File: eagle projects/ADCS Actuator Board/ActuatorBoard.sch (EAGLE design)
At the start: 155 parts, among them J19 TE_1-84953-1, J20 TE_1-84953-1, J21 TE_1-84953-1, J7 CNC_3221-10-0300-00, J8 CNC_3221-14-0300-00, U1 TVS991, U10 DRV10970_MOTOR_DRIVERDRV10970, U12 DRV10970_MOTOR_DRIVERDRV10970, U2 ADS7841E_2K5, U3 ADS7841E_2K5, U35 BD6210F-E2, U39 BD6210F-E2, U5 TVS991, U7 DRV10970_MOTOR_DRIVERDRV10970, U8 TVS991, U9 BD6210F-E2

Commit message: Staring REV B Act board
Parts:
- removed C119, C121, C122, C126, C129, C130, C139, C142, C25, C26: 0.1u, rcl:C-EUC0603
- removed C120, C140: 1u, rcl:C-EUC0603
- removed C123, C131: 0.1u, rcl:C-EUC0402
- removed C125, C141: 0.33u, rcl:C-EUC0603
- removed C127, C143: 2.2u, rcl:C-EUC0603
- removed C128, C144: 10u, rcl:C-EUC0603
- removed J19, J20, J21: TE_1-84953-1, my_library:TE_1-84953-1
- removed J5: (no value), my_library:PINHD-1X3
- removed JP7, JP9: (no value), my_library:JP1Q_
- removed JX, JY, JZ: (no value), my_library:TRM_BLK_1X2
- removed R23: 100R, rcl:R-US_M0805
- removed R28, R29, R37, R38, R5: 1.8k, rcl:R-US_R0402
- removed R3, R4, R76: 5.1k, rcl:R-US_R0402
- removed R73, R74: 3.3k, rcl:R-US_R0603
- removed TP35, TP36, TP43, TP44, TP46, TP54, TP7: TESTPOINT, my_library:TESTPOINT
- removed U1: TVS991, my_library:TVS991
- removed U35, U39, U9: BD6210F-E2, my_library:BD6210F-E2
- added C1, C11, C2, C20, C34, C45, C50, C51, C54, C58, C63: 0.1u, rcl:C-EUC0603
- added C10, C3, C4, C46, C52, C6, C8: 0.1u, rcl:C-EUC0402
- added C12, C32, C55, C62: 1u, rcl:C-EUC0603
- added C19, C57: 0.33u, rcl:C-EUC0603
- added C28, C35, C59: 2.2u, rcl:C-EUC0603
- added C30, C36, C60: 10u, rcl:C-EUC0603
- added C31, C38, C61: 0.01u, rcl:C-EUC0603
- added C5, C7, C9: 1u, rcl:C-EUC0402
- added J11, J2: TE_1-84953-1, my_library:TE_1-84953-1
- added J12, J3: (no value), my_library:PINHD-1X3
- added JP2, JP3: (no value), pinhead:PINHD-1X2
- added R102, R103, R59, R60: 10K, rcl:R-US_R0603
- added R104, R61: 75K, rcl:R-US_R0603
- added R105, R106, R62, R63: 3.3k, rcl:R-US_R0603
- added R107, R108, R109, R64, R65, R66: 4.7k, rcl:R-US_R0402
- added R110, R111, R112, R113, R114, R115, R58, R67, R68, R69, R70, R71, R75: 5.1M, rcl:R-US_R0402
- added R116, R77: 10k, rcl:R-US_R0603
- added R117, R78: 2k, rcl:R-US_R0603
- added R118, R79: 1k, rcl:R-US_R0603
- added R119, R80: 100k, rcl:R-US_R0603
- added R47, R89: 0R, rcl:R-US_M0805
- added R57: 10K, rcl:R-US_R0402
- added R81: 5.1k, rcl:R-US_R0402
- added R82: 100R, rcl:R-US_M0805
- added R88: DNP, rcl:R-US_M0805
- added TP1, TP10, TP11, TP12, TP13, TP14, TP15, TP16, TP17, TP18, TP19, TP20, TP26, TP27, TP28, TP29, TP33, TP37, TP38, TP39, TP47, TP48, TP49, TP50, TP53, TP55, TP56, TP57, TP58, TP59, TP60, TP61, TP62, TP63, TP8, TP9: TESTPOINT, my_library:TESTPOINT
- added U11, U18: BD6210F-E2, my_library:BD6210F-E2
- added U13, U17: LM2917MX/NOPB, my_library:LM2917MX/NOPB
- added U16, U6: DRV10970_MOTOR_DRIVERDRV10970, my_library:DRV10970_MOTOR_DRIVERDRV10970
- added U19: TSV991AILT, my_library:TSV991AILT
- added U4: ADS7841E_2K5, my_library:ADS7841E_2K5
- C27: device rcl:C-EUC0402 -> rcl:C-EUC0603
- C41: value 2.2u -> 1u
- C42: value 10u -> 0.1u
- J4: value (none) -> TE_1-84953-1; device my_library:PINHD-1X3 -> my_library:TE_1-84953-1
- JP5: device my_library:JP1Q_ -> pinhead:PINHD-1X2
- R1, R2: value 4.7k -> 10K; device rcl:R-US_R0402 -> rcl:R-US_R0603
- R11: value 4.7k -> 100R; device rcl:R-US_R0402 -> rcl:R-US_M0805
- R12: value 4.7k -> 5.1k
- R15: value 4.7k -> 1.8k
- R16: value 100R -> 1.8k; device rcl:R-US_M0805 -> rcl:R-US_R0402
- R17: value 5.1k -> 1.8k
- R19, R20: value 10K -> 4.7k; device rcl:R-US_R0603 -> rcl:R-US_R0402
- R21: value 75K -> 5.1M; device rcl:R-US_R0603 -> rcl:R-US_R0402
- R22: value 100R -> DNP
- R24: value 1.8k -> 0R; device rcl:R-US_R0402 -> rcl:R-US_M0805
- R25, R31: value 1.8k -> 5.1k
- R30: value 5.1k -> 100R; device rcl:R-US_R0402 -> rcl:R-US_M0805
- R35, R36: value 3.3k -> 5.1M; device rcl:R-US_R0603 -> rcl:R-US_R0402
- R41: value 5.1M -> 1.8k
- R42: value 5.1M -> DNP; device rcl:R-US_R0402 -> rcl:R-US_M0805
- R44: value 5.1M -> 10k; device rcl:R-US_R0402 -> rcl:R-US_R0603
- R48: value 10K -> 2k
- R49: value 10K -> 1k
- R7: value 4.7k -> 75K; device rcl:R-US_R0402 -> rcl:R-US_R0603
- R72: value 75K -> 100k
- R8, R9: value 4.7k -> 3.3k; device rcl:R-US_R0402 -> rcl:R-US_R0603
- R83: value 10K -> 5.1k; device rcl:R-US_R0603 -> rcl:R-US_R0402
- R84: value 10K -> 1.8k; device rcl:R-US_R0603 -> rcl:R-US_R0402
- R85: value 75K -> 1.8k; device rcl:R-US_R0603 -> rcl:R-US_R0402
- R86, R87: value 3.3k -> 1.8k; device rcl:R-US_R0603 -> rcl:R-US_R0402
- U10: value DRV10970_MOTOR_DRIVERDRV10970 -> LM2917MX/NOPB; device my_library:DRV10970_MOTOR_DRIVERDRV10970 -> my_library:LM2917MX/NOPB
- U12: value DRV10970_MOTOR_DRIVERDRV10970 -> TSV991AILT; device my_library:DRV10970_MOTOR_DRIVERDRV10970 -> my_library:TSV991AILT
- U5: value TVS991 -> BD6210F-E2; device my_library:TVS991 -> my_library:BD6210F-E2
- U8: value TVS991 -> TSV991AILT; device my_library:TVS991 -> my_library:TSV991AILT
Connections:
- removed net MAG_CUR_SEN_Y: R22.2, R30.2, U35.OUT1
- removed net MAG_CUR_SEN_Z: R16.2, R17.2, U39.OUT1
- removed net MAG_Y_FIN: TP43.TP, U35.FIN
- removed net N$10: R28.2, R76.1, U1.IN+
- removed net N$105: C139.1, U12.CPP
- removed net N$106: C140.2, U12.VCP
- removed net N$107: C139.2, U12.CPN
- removed net N$108: C143.1, U12.VINT
- removed net N$109: C141.1, U12.RETRY
- removed net N$18: R28.1, R37.1, R38.2
- removed net N$19 (its old number): R40.2, U10.DAA
- removed net N$23 (its old number): R43.1, U10.CMTMOD
- removed net N$3 (its old number): R39.2, U7.DAA
- removed net N$33: JP7.2, U35.OUT2
- removed net N$4: R5.1, R6.1, U8.IN-
- removed net N$67: JP9.2, U39.OUT2
- removed net N$7: R29.1, R4.1, U1.IN-
- removed net N$87: C119.1, U10.CPP
- removed net N$88: C120.2, U10.VCP
- removed net N$89: C119.2, U10.CPN
- removed net N$90: C127.1, U10.VINT
- removed net N$91: C125.1, U10.RETRY
- removed net OUT1_Y: JY.1, R22.1, R3.2
- removed net OUT1_Z: JZ.1, R16.1, R23.1, R4.2, R6.2
- removed net OUT2_Y: JP7.1, JY.2
- removed net OUT2_Z: JP9.1, JZ.2
- new net !CS!_SPD_SENSE_RW: J7.1, U4.!CS
- new net N$28: R21.2, U7.DAA
- new net N$29: R35.1, U7.CMTMOD
- new net N$30: C41.2, R72.2, TP13.TP, U10.CP2, U10.IN+
- new net N$31: R48.1, R49.2, U10.TACH-
- new net N$32: C8.1, R57.1, U4.!SHDN
- new net N$34: TP1.TP, U4.CH3
- new net N$35: R58.2, U4.BUSY
- new net N$36: C11.1, U6.CPP
- new net N$38: C12.2, U6.VCP
- new net N$39: C11.2, U6.CPN
- new net N$40: C28.1, U6.VINT
- new net N$41: C19.1, U6.RETRY
- new net N$43: R67.2, U6.DAA
- new net N$44: R68.1, U6.CMTMOD
- new net N$49: C32.2, R80.2, TP28.TP, U13.CP2, U13.IN+
- new net N$50: R78.1, R79.2, U13.TACH-
- new net N$51: C31.2, U13.CP1
- new net N$52: C38.2, U10.CP1
- new net N$53: R81.1, R84.2, U19.IN+
- new net N$54: R84.1, R86.1, R87.2
- new net N$55: R82.2, R88.2, R89.1
- new net N$63: C54.1, U16.CPP
- new net N$64: C55.2, U16.VCP
- new net N$65: C54.2, U16.CPN
- new net N$66: C59.1, U16.VINT
- new net N$68: C57.1, U16.RETRY
- new net N$69: R110.2, U16.DAA
- new net N$70: R111.1, U16.CMTMOD
- new net N$72: R117.1, R118.2, U17.TACH-
- new net N$73: C61.2, U17.CP1
- new net RW_X_SPD: R44.2, TP12.TP, U10.EMIT, U10.IN-, U4.CH1
- new net RW_Y_SPD: R116.2, TP56.TP, U17.EMIT, U17.IN-, U4.CH0
- new net RW_Z_SPD: R77.2, TP27.TP, U13.EMIT, U13.IN-, U4.CH2
- new net X_DNC_1: R36.1, U10.DNC_1
- new net X_DNC_2: R39.1, U10.DNC_2
- new net X_DNC_3: R43.1, U10.DNC_3
- new net X_DNC_4: R40.1, U10.DNC_4
- new net Y_DNC_1: R112.1, U17.DNC_1
- new net Y_DNC_2: R113.1, U17.DNC_2
- new net Y_DNC_3: R115.1, U17.DNC_3
- new net Y_DNC_4: R114.1, U17.DNC_4
- new net Z_DNC_1: R69.1, U13.DNC_1
- new net Z_DNC_2: R70.1, U13.DNC_2
- new net Z_DNC_3: R75.1, U13.DNC_3
- new net Z_DNC_4: R71.1, U13.DNC_4
- net +3V3: now also C10.1, C34.2, C4.1, C42.2, C5.1, C6.1, C63.2, C7.1, C9.1, R105.1, R106.1, R118.1, R17.2, R34.2, R49.1, R57.2, R62.1, R63.1, R79.1, R8.1, R86.2, R9.1, U10.COL, U10.V+, U13.COL, U13.V+, U17.COL, U17.V+, U4.VCC+, U4.VCC+_2, U4.VREF; no longer R31.2, R33.2, R35.1, R36.1, R37.2, R73.1, R74.1, R86.1, R87.1
- net +5V: now also C1.1, C12.1, C2.2, C3.1, C30.1, C36.1, C45.2, C46.1, C50.1, C51.2, C52.1, C55.1, C60.1, J11.1, J12.3, J2.1, J3.3, J4.1, R102.2, R107.2, R108.2, R109.2, R20.2, R59.2, R64.2, R65.2, R66.2, U11.VCC_1, U11.VCC_2, U11.VREF, U12.VCC, U16.VM, U18.VCC_1, U18.VCC_2, U18.VREF, U19.VCC, U5.VCC_1, U5.VCC_2, U5.VREF, U6.VM; no longer C120.1, C121.1, C122.2, C123.1, C128.1, C129.1, C130.2, C131.1, C140.1, C144.1, C25.1, C26.2, C42.1, J19.1, J20.1, J21.1, J4.3, J5.3, R11.2, R12.2, R15.2, R2.2, R48.2, R7.2, R8.2, R83.2, R9.2, U1.VCC, U10.VM, U12.VM, U35.VCC_1, U35.VCC_2, U35.VREF, U39.VCC_1, U39.VCC_2, U39.VREF, U5.VCC, U9.VCC_1, U9.VCC_2, U9.VREF
- net BRKMOD_X: now also J6.2, U7.BRKMOD; no longer J4.2, U10.BRKMOD
- net BRKMOD_Y: now also J12.2, U16.BRKMOD; no longer J6.2, U7.BRKMOD
- net BRKMOD_Z: now also J3.2, U6.BRKMOD; no longer J5.2, U12.BRKMOD
- net CUR_OUT1: no longer R5.2, U8.OUT
- net CUR_OUT2: no longer R24.2, TP46.TP, U5.OUT
- net CUR_OUT3: now also R16.2, R33.2, R85.2, TP10.TP, TP30.TP, TP51.TP, U12.OUT, U19.OUT, U8.OUT; no longer R29.2, TP54.TP, U1.OUT
- net GND: now also C1.2, C10.2, C19.2, C2.1, C20.2, C28.2, C3.2, C30.2, C31.1, C32.1, C34.1, C35.2, C36.2, C38.1, C4.2, C41.1, C42.1, C45.1, C46.2, C5.2, C50.2, C51.1, C52.2, C57.2, C58.2, C59.2, C6.2, C60.2, C61.1, C62.1, C63.1, C7.2, C8.2, C9.2, J11.5, J11.TAB1, J11.TAB2, J12.1, J2.5, J2.TAB1, J2.TAB2, J3.1, J4.5, J4.TAB1, J4.TAB2, R103.1, R104.1, R110.1, R111.2, R112.2, R113.2, R114.2, R115.2, R116.1, R117.2, R119.1, R18.1, R2.1, R35.2, R36.2, R39.2, R40.2, R44.1, R48.2, R58.1, R60.1, R61.1, R67.1, R68.2, R69.2, R7.1, R70.2, R71.2, R75.2, R77.1, R78.2, R80.1, R87.1, U11.GND, U12.VSS, U13.GND, U16.GND, U16.THERMALPAD, U17.GND, U18.GND, U19.VSS, U4.COM, U4.GND, U4.MODE, U5.GND, U6.GND, U6.THERMALPAD; no longer C121.2, C122.1, C123.2, C125.2, C126.2, C127.2, C128.2, C129.2, C130.1, C131.2, C141.2, C142.2, C143.2, C144.2, C25.2, C26.1, C41.2, C42.2, J19.5, J19.TAB1, J19.TAB2, J20.5, J20.TAB1, J20.TAB2, J21.5, J21.TAB1, J21.TAB2, J4.1, J5.1, R20.1, R32.1, R34.1, R38.1, R39.1, R40.1, R42.2, R44.2, R49.1, R84.1, R85.1, U1.VSS, U10.THERMALPAD, U12.GND, U12.THERMALPAD, U35.GND, U39.GND, U5.VSS, U9.GND
- net MAG_CUR_SEN_X: now also R24.2, R25.2, R47.2, R6.2, R81.2, R89.2, TP17.TP, TP34.TP, TP52.TP, U11.OUT1, U18.OUT1, U5.OUT1; no longer R23.2, R76.2, U9.OUT1
- net MAG_X_FIN: now also TP24.TP, TP47.TP, TP8.TP, U11.FIN, U18.FIN, U5.FIN; no longer TP35.TP, U9.FIN
- net MAG_X_RIN: now also TP25.TP, TP48.TP, TP9.TP, U11.RIN, U18.RIN, U5.RIN; no longer TP36.TP, U9.RIN
- net MAG_Y_RIN: no longer TP44.TP, U35.RIN
- net MAG_Z_FIN: no longer TP51.TP, U39.FIN
- net MAG_Z_RIN: no longer TP52.TP, U39.RIN
- net N$16: now also R11.2, R22.2, R24.1; no longer JP5.2, U9.OUT2
- net N$17: now also R31.1, U12.IN-; no longer R34.2
- net N$20: now also R25.1, R32.2, U12.IN+; no longer R41.2, U12.DAA
- net N$21: now also R32.1, R34.1, R41.2; no longer R18.1, R31.1, R32.2
- net N$22: now also R30.2, R42.2, R47.1; no longer R42.1, U12.CMTMOD
- net N$24: now also C35.1, U7.VINT; no longer R44.1, U7.CMTMOD
- net N$48: now also R83.1, R85.1, U19.IN-; no longer R25.1
- net N$6: now also R12.1, R16.1, U8.IN-; no longer R24.1, R3.1, U5.IN-
- net N$71: now also C62.2, R119.2, TP57.TP, U17.CP2, U17.IN+; no longer C41.1, U7.VINT
- net N$8: now also R15.2, R6.1; no longer R17.1, R18.2
- net N$9: now also R15.1, R17.1, R18.2; no longer R25.2, R30.1, U5.IN+
- net OUT1_X: now also JP2.1, JP3.1, JP5.1, R11.1, R12.2, R22.1, R30.1, R31.2, R42.1, R82.1, R83.2, R88.1, TP21.TP, TP39.TP, TP62.TP; no longer JX.1
- net OUT2_X: now also JP2.2, JP3.2, JP5.2, TP22.TP, TP40.TP, TP63.TP, U11.OUT2, U18.OUT2, U5.OUT2; no longer JP5.1, JX.2
- net RW_X_DIR: now also U7.FR; no longer U10.FR
- net RW_X_I_SENS: now also R7.2, TP11.TP, U7.CS; no longer R72.2, TP34.TP, U10.CS
- net RW_X_LOCK: now also R9.2, U7.RD; no longer R74.2, U10.RD
- net RW_X_OUTFG: now also R8.2, TP23.TP, U10.TACH+, U7.FG; no longer J8.13, R73.2, U10.FG
- net RW_X_SPEED_CTRL: now also U7.PWM; no longer U10.PWM
- net RW_Y_DIR: now also U16.FR; no longer U7.FR
- net RW_Y_I_SENS: now also R104.2, TP55.TP, U16.CS; no longer R21.2, TP30.TP, U7.CS
- net RW_Y_LOCK: now also R106.2, U16.RD; no longer R36.2, U7.RD
- net RW_Y_OUTFG: now also R105.2, TP61.TP, U16.FG, U17.TACH+; no longer J7.1, R35.2, U7.FG
- net RW_Y_SPEED_CTRL: now also U16.PWM; no longer U7.PWM
- net RW_Z_DIR: now also U6.FR; no longer U12.FR
- net RW_Z_I_SENS: now also R61.2, TP26.TP, U6.CS; no longer R85.2, TP40.TP, U12.CS
- net RW_Z_LOCK: now also R63.2, U6.RD; no longer R87.2, U12.RD
- net RW_Z_OUTFG: now also R62.2, TP38.TP, U13.TACH+, U6.FG; no longer J7.2, R86.2, U12.FG
- net RW_Z_SPEED_CTRL: now also U6.PWM; no longer U12.PWM
- net UCB0_SPI_CLK: now also U4.DCLK
- net UCB0_SPI_MISO: now also U4.DOUT
- net UCB0_SPI_MOSI: now also U4.DIN
- net VINT/2_X: now also C16.1, R1.1, R2.2, U7.U_HN, U7.V_HN, U7.W_HN; no longer C126.1, R48.1, R49.2, U10.U_HN, U10.V_HN, U10.W_HN
- net VINT/2_Y: now also C58.1, R102.1, R103.2, U16.U_HN, U16.V_HN, U16.W_HN; no longer C16.1, R19.1, R20.2, U7.U_HN, U7.V_HN, U7.W_HN
- net VINT/2_Z: now also C20.1, R59.1, R60.2, U6.U_HN, U6.V_HN, U6.W_HN; no longer C142.1, R83.1, R84.2, U12.U_HN, U12.V_HN, U12.W_HN
- net X_HALL_A: now also J4.3, R19.1, U7.U_HP; no longer J19.3, R2.1, U10.U_HP
- net X_HALL_B: now also J4.4, R10.1, U7.V_HP; no longer J19.4, R1.1, U10.V_HP
- net X_HALL_C: now also J4.2, R20.1, U7.W_HP; no longer J19.2, R7.1, U10.W_HP
- net X_PHASE_A: now also J4.10, J4.11, TP14.TP, U7.U; no longer J19.10, J19.11, U10.U
- net X_PHASE_B: now also J4.8, J4.9, TP15.TP, U7.V; no longer J19.8, J19.9, U10.V
- net X_PHASE_C: now also U7.W; no longer J19.6, J19.7, U10.W
- net Y_HALL_A: now also J11.3, R108.1, TP53.TP, U16.U_HP; no longer J20.3, R9.1, TP25.TP, U7.U_HP
- net Y_HALL_B: now also J11.4, R107.1, TP50.TP, U16.V_HP; no longer J20.4, R8.1, TP24.TP, U7.V_HP
- net Y_HALL_C: now also J11.2, R109.1, TP49.TP, U16.W_HP; no longer J20.2, R10.1, TP23.TP, U7.W_HP
- net Y_PHASE_A: now also J11.10, J11.11, TP58.TP, U16.U; no longer J20.10, J20.11, U7.U
- net Y_PHASE_B: now also J11.8, J11.9, TP59.TP, U16.V; no longer J20.8, J20.9, U7.V
- net Y_PHASE_C: now also J11.6, J11.7, TP60.TP, U16.W; no longer J20.6, J20.7, U7.W
- net Z_HALL_A: now also J2.3, R65.1, TP20.TP, U6.U_HP; no longer J21.3, R12.1, TP22.TP, U12.U_HP
- net Z_HALL_B: now also J2.4, R64.1, TP19.TP, U6.V_HP; no longer J21.4, R11.1, TP21.TP, U12.V_HP
- net Z_HALL_C: now also J2.2, R66.1, TP18.TP, U6.W_HP; no longer J21.2, R15.1, TP7.TP, U12.W_HP
- net Z_PHASE_A: now also J2.10, J2.11, TP29.TP, U6.U; no longer J21.10, J21.11, U12.U
- net Z_PHASE_B: now also J2.8, J2.9, TP33.TP, U6.V; no longer J21.8, J21.9, U12.V
- net Z_PHASE_C: now also J2.6, J2.7, J4.6, J4.7, TP16.TP, TP37.TP, U6.W; no longer J21.6, J21.7, U12.W
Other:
- note added: "Brake-mode select jumper"
- note added: "DNC pins pulled to ground with large res to prevent charge buildup in orbit."
- note added: "Device measures frequency of zero-crossings at TACH- level = 1/3*Vcc = 1 V"
- note added: "MQTR-Connector"
- note added: "RW_X_LOCK"
- note added: "Vout = R56 * C2 * Vcc * f"
- note added: "Vout = R72 * C41 * Vcc * f"
- note added: "freq in ->"
- note removed: "Hall sensors on Maxon motor require external pull-up resistor"

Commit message: Added FV converters, replaced connectors
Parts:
- removed C10, C17, C21, C23, C29, C37, C39, C4, C43, C56, C6, C8: 0.1u, rcl:C-EUC0402
- removed C18, C22, C24, C33, C40, C44, C5, C7, C9: 1u, rcl:C-EUC0402
- removed J7: CNC_3221-10-0300-00, my_library:CNC_3221-10-0300-00
- removed J8: CNC_3221-14-0300-00, my_library:CNC_3221-14-0300-00
- removed R13, R14, R57: 10K, rcl:R-US_R0402
- removed R45, R46, R58: 5.1M, rcl:R-US_R0402
- removed TP1, TP31, TP32: TESTPOINT, my_library:TESTPOINT
- removed U2, U3, U4: ADS7841E_2K5, my_library:ADS7841E_2K5
- added C65, C67, C69, C71, C72, C74, C76, C78, C86, C88, C90, C92: 0.1u, rcl:C-EUC0402
- added C66, C68, C70, C73, C75, C77, C87, C89, C91: 1u, rcl:C-EUC0402
- added JP1: (no value), pinhead:PINHD-2X12
- added R23, R3, R37, R51: 5.1M, rcl:R-US_R0402
- added R29, R5, R50: 10K, rcl:R-US_R0402
- added U14, U20, U9: ADS7841E_2K5, my_library:ADS7841E_2K5
- R17, R34, R86: value 1.8k -> 2.2k
- R18, R41, R87: value 1.8k -> 1.1k
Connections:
- removed net MAG_Y_FIN\: J8.6
- removed net N$11: C23.1, R14.1, U3.!SHDN
- removed net N$12: TP32.TP, U3.CH3
- removed net N$13: C43.1, R13.1, U2.!SHDN
- removed net N$15: TP31.TP, U2.CH3
- removed net N$2: R46.2, U3.BUSY
- removed net N$32: C8.1, R57.1, U4.!SHDN
- removed net N$34: TP1.TP, U4.CH3
- removed net N$35: R58.2, U4.BUSY
- removed net N$37: J7.10
- removed net N$42: J7.9
- new net MAG_CUR_SEN_Y: R25.2, R47.2, TP34.TP, U11.OUT1
- new net MAG_CUR_SEN_Z: R81.2, R89.2, TP52.TP, U18.OUT1
- new net MAG_Y_FIN: JP1.12, TP24.TP, U11.FIN
- new net N$18: C69.1, R5.1, U9.!SHDN
- new net N$25: R23.2, U9.BUSY
- new net N$26: U9.CH3
- new net N$33: C76.1, R29.1, U14.!SHDN
- new net N$45: R37.2, U14.BUSY
- new net N$46: U14.CH3
- new net N$58: C90.1, R50.1, U20.!SHDN
- new net N$59: R51.2, U20.BUSY
- new net N$60: U20.CH3
- new net OUT1_Y: JP3.1, R30.1, R31.2, R42.1, TP39.TP
- new net OUT1_Z: JP5.1, R82.1, R83.2, R88.1, TP62.TP
- new net OUT2_Y: JP3.2, TP40.TP, U11.OUT2
- new net OUT2_Z: JP5.2, TP63.TP, U18.OUT2
- net !CS!_CURR_SENSE_MTQR: now also JP1.23, U9.!CS; no longer J7.5, U2.!CS
- net !CS!_CURR_SENSE_RW: now also JP1.21, U14.!CS; no longer J7.3, U3.!CS
- net !CS!_SPD_SENSE_RW: now also JP1.24, U20.!CS; no longer J7.1, U4.!CS
- net +3V3: now also C65.1, C66.1, C67.1, C68.1, C70.1, C71.1, C72.1, C73.1, C74.1, C75.1, C77.1, C78.1, C86.1, C87.1, C88.1, C89.1, C91.1, C92.1, JP1.1, R29.2, R5.2, R50.2, U14.VCC+, U14.VCC+_2, U14.VREF, U20.VCC+, U20.VCC+_2, U20.VREF, U9.VCC+, U9.VCC+_2, U9.VREF; no longer C10.1, C17.1, C18.1, C21.1, C22.1, C24.1, C29.1, C33.1, C37.1, C39.1, C4.1, C40.1, C44.1, C5.1, C56.1, C6.1, C7.1, C9.1, J7.7, R13.2, R14.2, R17.2, R34.2, R57.2, R86.2, U2.VCC+, U2.VCC+_2, U2.VREF, U3.VCC+, U3.VCC+_2, U3.VREF, U4.VCC+, U4.VCC+_2, U4.VREF
- net +5V: now also JP1.2, R17.2, R34.2, R86.2; no longer J8.14
- net CUR_OUT1: now also R16.2, TP10.TP, U8.OUT, U9.CH0; no longer U2.CH0
- net CUR_OUT2: now also R33.2, TP30.TP, U12.OUT, U9.CH1; no longer U2.CH1
- net CUR_OUT3: now also U9.CH2; no longer R16.2, R33.2, TP10.TP, TP30.TP, U12.OUT, U2.CH2, U8.OUT
- net GND: now also C65.2, C66.2, C67.2, C68.2, C69.2, C70.2, C71.2, C72.2, C73.2, C74.2, C75.2, C76.2, C77.2, C78.2, C86.2, C87.2, C88.2, C89.2, C90.2, C91.2, C92.2, R23.1, R3.1, R37.1, R51.1, U14.COM, U14.GND, U14.MODE, U20.COM, U20.GND, U20.MODE, U9.COM, U9.GND, U9.MODE; no longer C10.2, C17.2, C18.2, C21.2, C22.2, C23.2, C24.2, C29.2, C33.2, C37.2, C39.2, C4.2, C40.2, C43.2, C44.2, C5.2, C56.2, C6.2, C7.2, C8.2, C9.2, R45.2, R46.1, R58.1, U2.COM, U2.GND, U2.MODE, U3.COM, U3.GND, U3.MODE, U4.COM, U4.GND, U4.MODE
- net MAG_CUR_SEN_X: no longer R25.2, R47.2, R81.2, R89.2, TP34.TP, TP52.TP, U11.OUT1, U18.OUT1
- net MAG_X_FIN: now also JP1.8; no longer J8.10, TP24.TP, TP47.TP, U11.FIN, U18.FIN
- net MAG_X_RIN: now also JP1.6; no longer J8.12, TP25.TP, TP48.TP, U11.RIN, U18.RIN
- net MAG_Y_RIN: now also JP1.10, TP25.TP, U11.RIN; no longer J8.8
- net MAG_Z_FIN: now also JP1.16, TP47.TP, U18.FIN; no longer J8.2
- net MAG_Z_RIN: now also JP1.14, TP48.TP, U18.RIN; no longer J8.4
- net N$1: now also JP1.4, R3.2; no longer R45.1, U2.BUSY
- net OUT1_X: no longer JP3.1, JP5.1, R30.1, R31.2, R42.1, R82.1, R83.2, R88.1, TP39.TP, TP62.TP
- net OUT2_X: no longer JP3.2, JP5.2, TP40.TP, TP63.TP, U11.OUT2, U18.OUT2
- net RW_X_DIR: now also JP1.13; no longer J8.7
- net RW_X_I_SENS: now also U14.CH1; no longer U3.CH1
- net RW_X_LOCK: now also JP1.9
- net RW_X_SPD: now also U20.CH1; no longer U4.CH1
- net RW_X_SPEED_CTRL: now also JP1.11; no longer J8.1
- net RW_Y_DIR: now also JP1.19; no longer J8.9
- net RW_Y_I_SENS: now also U14.CH2; no longer U3.CH0
- net RW_Y_LOCK: now also JP1.15
- net RW_Y_SPD: now also U20.CH0; no longer U4.CH0
- net RW_Y_SPEED_CTRL: now also JP1.17; no longer J8.3
- net RW_Z_DIR: now also JP1.7; no longer J8.11
- net RW_Z_I_SENS: now also U14.CH0; no longer U3.CH2
- net RW_Z_LOCK: now also JP1.3
- net RW_Z_SPD: now also U20.CH2; no longer U4.CH2
- net RW_Z_SPEED_CTRL: now also JP1.5; no longer J8.5
- net UCB0_SPI_CLK: now also JP1.18, U14.DCLK, U20.DCLK, U9.DCLK; no longer J7.4, U2.DCLK, U3.DCLK, U4.DCLK
- net UCB0_SPI_MISO: now also JP1.22, U14.DOUT, U20.DOUT, U9.DOUT; no longer J7.6, U2.DOUT, U3.DOUT, U4.DOUT
- net UCB0_SPI_MOSI: now also JP1.20, U14.DIN, U20.DIN, U9.DIN; no longer J7.8, U2.DIN, U3.DIN, U4.DIN
- net X_PHASE_C: now also J4.6, J4.7, TP16.TP
- net Z_PHASE_C: no longer J4.6, J4.7, TP16.TP
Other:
- note added: "Amplifier biased to 3.3V/2"
- note added: "DNP = do not populate"
- note added: "Note! Check that output gain is tuned for 0 to 3.3V"
- note added: "Use low tolerance resistors <1% to ensure linear amplifier output"
- note removed: "RW_X_LOCK"

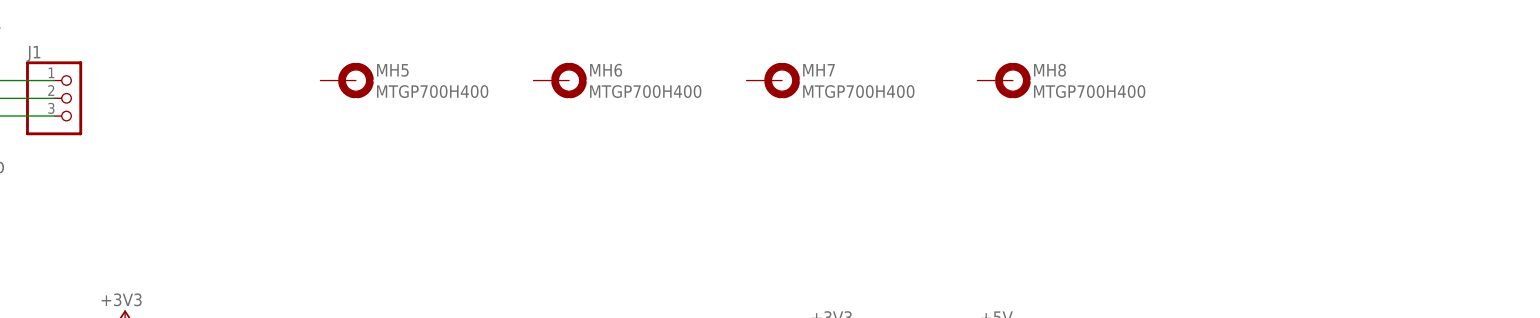
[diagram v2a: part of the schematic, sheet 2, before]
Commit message: Added power connector and mobo-act brd mounting holes
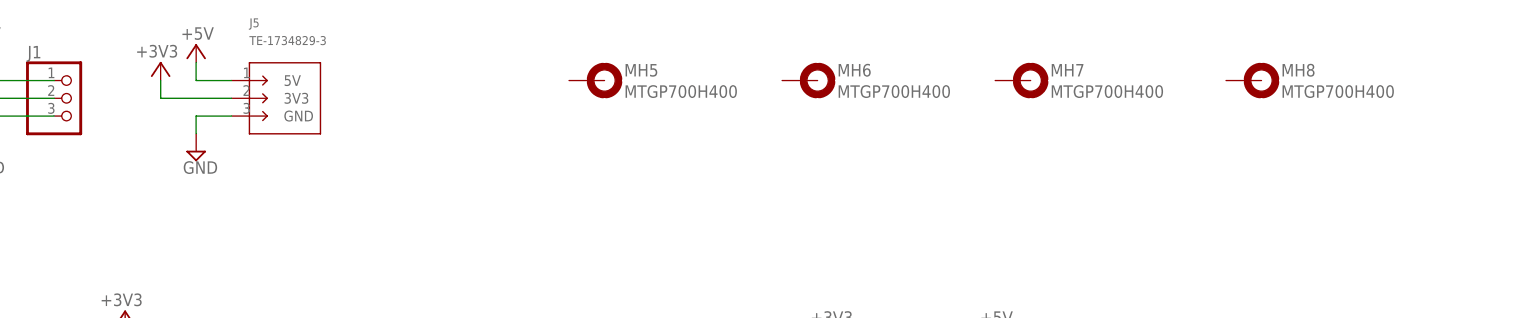
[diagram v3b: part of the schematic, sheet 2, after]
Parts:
- added J5: TE-1734829-3, my_library:TE-1734829-3
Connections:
- net +3V3: now also J5.3V3
- net +5V: now also J5.5V
- net GND: now also J5.GND
- net RW_Y_SPD: now also U20.CH2; no longer U20.CH0
- net RW_Z_SPD: now also U20.CH0; no longer U20.CH2
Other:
- moved on the sheet: MH5, MH6, MH7, MH8
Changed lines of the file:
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@@
 <part name="SUPPLY23" library="supply2" library_urn="urn:adsk.eagle:library:372" deviceset="GND" device=""/>
 <part name="SUPPLY26" library="supply2" library_urn="urn:adsk.eagle:library:372" deviceset="GND" device=""/>
+<part name="J5" library="my_library" library_urn="urn:adsk.eagle:library:22876504" deviceset="TE-1734829-3" device="" package3d_urn="urn:adsk.eagle:package:27602903/2"/>
+<part name="P+19" library="supply1" library_urn="urn:adsk.eagle:library:371" deviceset="+5V" device=""/>
+<part name="+3V1" library="supply1" library_urn="urn:adsk.eagle:library:371" deviceset="+3V3" device=""/>
+<part name="SUPPLY30" library="supply2" library_urn="urn:adsk.eagle:library:372" deviceset="GND" device=""/>
 </parts>
 <sheets>
@@
 </plain>
 <instances>
-<instance part="MH5" gate="G$1" x="86.36" y="190.5" smashed="yes" grouprefs="BOARD_MOUNTING_HOLES">
-<attribute name="NAME" x="89.154" y="191.0842" size="1.778" layer="95"/>
-<attribute name="VALUE" x="89.154" y="188.0362" size="1.778" layer="96"/>
-</instance>
-<instance part="MH6" gate="G$1" x="116.84" y="190.5" smashed="yes" grouprefs="BOARD_MOUNTING_HOLES">
-<attribute name="NAME" x="119.634" y="191.0842" size="1.778" layer="95"/>
-<attribute name="VALUE" x="119.634" y="188.0362" size="1.778" layer="96"/>
-</instance>
-<instance part="MH7" gate="G$1" x="147.32" y="190.5" smashed="yes" grouprefs="BOARD_MOUNTING_HOLES">
-<attribute name="NAME" x="150.114" y="191.0842" size="1.778" layer="95"/>
-<attribute name="VALUE" x="150.114" y="188.0362" size="1.778" layer="96"/>
-</instance>
-<instance part="MH8" gate="G$1" x="180.34" y="190.5" smashed="yes" grouprefs="BOARD_MOUNTING_HOLES">
-<attribute name="NAME" x="183.134" y="191.0842" size="1.778" layer="95"/>
-<attribute name="VALUE" x="183.134" y="188.0362" size="1.778" layer="96"/>
+<instance part="MH5" gate="G$1" x="121.92" y="190.5" smashed="yes" grouprefs="BOARD_MOUNTING_HOLES">
+<attribute name="NAME" x="124.714" y="191.0842" size="1.778" layer="95"/>
+<attribute name="VALUE" x="124.714" y="188.0362" size="1.778" layer="96"/>
+</instance>
+<instance part="MH6" gate="G$1" x="152.4" y="190.5" smashed="yes" grouprefs="BOARD_MOUNTING_HOLES">
+<attribute name="NAME" x="155.194" y="191.0842" size="1.778" layer="95"/>
+<attribute name="VALUE" x="155.194" y="188.0362" size="1.778" layer="96"/>
+</instance>
+<instance part="MH7" gate="G$1" x="182.88" y="190.5" smashed="yes" grouprefs="BOARD_MOUNTING_HOLES">
+<attribute name="NAME" x="185.674" y="191.0842" size="1.778" layer="95"/>
+<attribute name="VALUE" x="185.674" y="188.0362" size="1.778" layer="96"/>
+</instance>
+<instance part="MH8" gate="G$1" x="215.9" y="190.5" smashed="yes" grouprefs="BOARD_MOUNTING_HOLES">
+<attribute name="NAME" x="218.694" y="191.0842" size="1.778" layer="95"/>
+<attribute name="VALUE" x="218.694" y="188.0362" size="1.778" layer="96"/>
 </instance>
 <instance part="J1" gate="A" x="45.72" y="187.96" smashed="yes" grouprefs="POWER">
@@
 <attribute name="VALUE" x="147.955" y="22.225" size="1.778" layer="96"/>
 </instance>
+<instance part="J5" gate="G$1" x="73.66" y="187.96" smashed="yes">
+<attribute name="NAME" x="71.12" y="198.12" size="1.27" layer="95"/>
+<attribute name="VALUE" x="71.12" y="195.58" size="1.27" layer="96"/>
+</instance>
+<instance part="P+19" gate="1" x="63.5" y="195.58" smashed="yes">
+<attribute name="VALUE" x="66.04" y="198.12" size="1.778" layer="96" rot="R180"/>
+</instance>
+<instance part="+3V1" gate="G$1" x="58.42" y="193.04" smashed="yes">
+<attribute name="VALUE" x="60.96" y="195.58" size="1.778" layer="96" rot="R180"/>
+</instance>
+<instance part="SUPPLY30" gate="GND" x="63.5" y="180.34" smashed="yes">
+<attribute name="VALUE" x="61.595" y="177.165" size="1.778" layer="96"/>
+</instance>
 </instances>
 <busses>
@@
 <wire x1="200.66" y1="149.86" x2="198.12" y2="149.86" width="0.1524" layer="91"/>
 </segment>
+<segment>
+<pinref part="SUPPLY30" gate="GND" pin="GND"/>
+<wire x1="63.5" y1="182.88" x2="63.5" y2="185.42" width="0.1524" layer="91"/>
+<pinref part="J5" gate="G$1" pin="GND"/>
+<wire x1="63.5" y1="185.42" x2="68.58" y2="185.42" width="0.1524" layer="91"/>
+</segment>
 </net>
 <net name="UCB0_SPI_MOSI" class="0">
@@
 <wire x1="177.8" y1="147.32" x2="177.8" y2="152.4" width="0.1524" layer="91"/>
 </segment>
+<segment>
+<pinref part="P+19" gate="1" pin="+5V"/>
+<wire x1="63.5" y1="193.04" x2="63.5" y2="190.5" width="0.1524" layer="91"/>
+<pinref part="J5" gate="G$1" pin="5V"/>
+<wire x1="63.5" y1="190.5" x2="68.58" y2="190.5" width="0.1524" layer="91"/>
+</segment>
 </net>
 <net name="+3V3" class="0">
@@
 <wire x1="154.94" y1="147.32" x2="162.56" y2="147.32" width="0.1524" layer="91"/>
 </segment>
+<segment>
+<pinref part="J5" gate="G$1" pin="3V3"/>
+<wire x1="68.58" y1="187.96" x2="58.42" y2="187.96" width="0.1524" layer="91"/>
+<pinref part="+3V1" gate="G$1" pin="+3V3"/>
+<wire x1="58.42" y1="187.96" x2="58.42" y2="190.5" width="0.1524" layer="91"/>
+</segment>
 </net>
 <net name="MAG_Z_FIN" class="0">
@@
 </segment>
 </net>
-<net name="RW_Z_SPD" class="0">
+<net name="RW_Y_SPD" class="0">
 <segment>
 <pinref part="U20" gate="A" pin="CH2"/>
@@
 </segment>
 </net>
-<net name="RW_Y_SPD" class="0">
-<segment>
-<pinref part="U20" gate="A" pin="CH0"/>
-<wire x1="109.22" y1="104.14" x2="104.14" y2="104.14" width="0.1524" layer="91"/>
-<label x="104.14" y="104.14" size="1.778" layer="95" rot="MR0"/>
-</segment>
-</net>
-<net name="RW_X_SPD" class="0">
-<segment>
-<pinref part="U20" gate="A" pin="CH1"/>
-<wire x1="109.22" y1="101.6" x2="104.14" y2="101.6" width="0.1524" layer="91"/>
-<label x="104.14" y="101.6" size="1.778" layer="95" rot="MR0"/>
-</segment>
-</net>
 <net name="N$33" class="0">
 <segment>
@@
 </segment>
 </net>
+<net name="RW_Z_SPD" class="0">
+<segment>
+<pinref part="U20" gate="A" pin="CH0"/>
+<wire x1="109.22" y1="104.14" x2="104.14" y2="104.14" width="0.1524" layer="91"/>
+<label x="104.14" y="104.14" size="1.778" layer="95" rot="MR0"/>
+</segment>
+</net>
+<net name="RW_X_SPD" class="0">
+<segment>
+<pinref part="U20" gate="A" pin="CH1"/>
+<wire x1="109.22" y1="101.6" x2="104.14" y2="101.6" width="0.1524" layer="91"/>
+<label x="104.14" y="101.6" size="1.778" layer="95" rot="MR0"/>
+</segment>
+</net>

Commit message: Rev B almost ready
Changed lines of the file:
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@@
 </segment>
 </net>
-<net name="N$18" class="0">
-<segment>
-<pinref part="C69" gate="G$1" pin="1"/>
-<pinref part="R5" gate="G$1" pin="1"/>
-<pinref part="U9" gate="A" pin="!SHDN"/>
-<wire x1="149.86" y1="40.64" x2="129.54" y2="40.64" width="0.1524" layer="91"/>
-<junction x="139.7" y="40.64"/>
-<wire x1="149.86" y1="40.64" x2="139.7" y2="40.64" width="0.1524" layer="91"/>
-</segment>
-</net>
 <net name="N$25" class="0">
 <segment>
@@
 </segment>
 </net>
+<net name="N$2" class="0">
+<segment>
+<pinref part="U9" gate="A" pin="!SHDN"/>
+<pinref part="R5" gate="G$1" pin="1"/>
+<wire x1="129.54" y1="40.64" x2="139.7" y2="40.64" width="0.1524" layer="91"/>
+<pinref part="C69" gate="G$1" pin="1"/>
+<wire x1="139.7" y1="40.64" x2="149.86" y2="40.64" width="0.1524" layer="91"/>
+<junction x="139.7" y="40.64"/>
+</segment>
+</net>
 </nets>
 </sheet>
@@
 </segment>
 </net>
-<net name="N$33" class="0">
-<segment>
-<pinref part="C76" gate="G$1" pin="1"/>
-<pinref part="R29" gate="G$1" pin="1"/>
-<pinref part="U14" gate="A" pin="!SHDN"/>
-<wire x1="185.42" y1="152.4" x2="165.1" y2="152.4" width="0.1524" layer="91"/>
-<junction x="175.26" y="152.4"/>
-<wire x1="185.42" y1="152.4" x2="175.26" y2="152.4" width="0.1524" layer="91"/>
-</segment>
-</net>
 <net name="N$45" class="0">
 <segment>
@@
 </segment>
 </net>
-<net name="N$58" class="0">
-<segment>
-<pinref part="C90" gate="G$1" pin="1"/>
-<pinref part="R50" gate="G$1" pin="1"/>
-<pinref part="U20" gate="A" pin="!SHDN"/>
-<wire x1="185.42" y1="88.9" x2="165.1" y2="88.9" width="0.1524" layer="91"/>
-<junction x="175.26" y="88.9"/>
-<wire x1="185.42" y1="88.9" x2="175.26" y2="88.9" width="0.1524" layer="91"/>
-</segment>
-</net>
 <net name="N$59" class="0">
 <segment>
@@
 </segment>
 </net>
+<net name="N$4" class="0">
+<segment>
+<pinref part="U14" gate="A" pin="!SHDN"/>
+<pinref part="R29" gate="G$1" pin="1"/>
+<wire x1="165.1" y1="152.4" x2="175.26" y2="152.4" width="0.1524" layer="91"/>
+<pinref part="C76" gate="G$1" pin="1"/>
+<wire x1="175.26" y1="152.4" x2="185.42" y2="152.4" width="0.1524" layer="91"/>
+<junction x="175.26" y="152.4"/>
+</segment>
+</net>
+<net name="N$7" class="0">
+<segment>
+<pinref part="U20" gate="A" pin="!SHDN"/>
+<pinref part="R50" gate="G$1" pin="1"/>
+<wire x1="165.1" y1="88.9" x2="175.26" y2="88.9" width="0.1524" layer="91"/>
+<pinref part="C90" gate="G$1" pin="1"/>
+<wire x1="175.26" y1="88.9" x2="185.42" y2="88.9" width="0.1524" layer="91"/>
+<junction x="175.26" y="88.9"/>
+</segment>
+</net>
